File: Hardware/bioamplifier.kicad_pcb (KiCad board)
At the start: 4 copper layers, 71.8 x 45.1 mm, 97 parts, among them J1 Conn_01x07_Socket, J2 Conn_01x26_Pin, J3 Conn_01x07_Socket, J4 Jumper, J5 Jumper, U1 ADS1299IPAG, U10 TPD4E1B06DCKR, U11 LM2665M6, U2 TPD4E1B06DCKR, U3 TPD4E1B06DCKR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

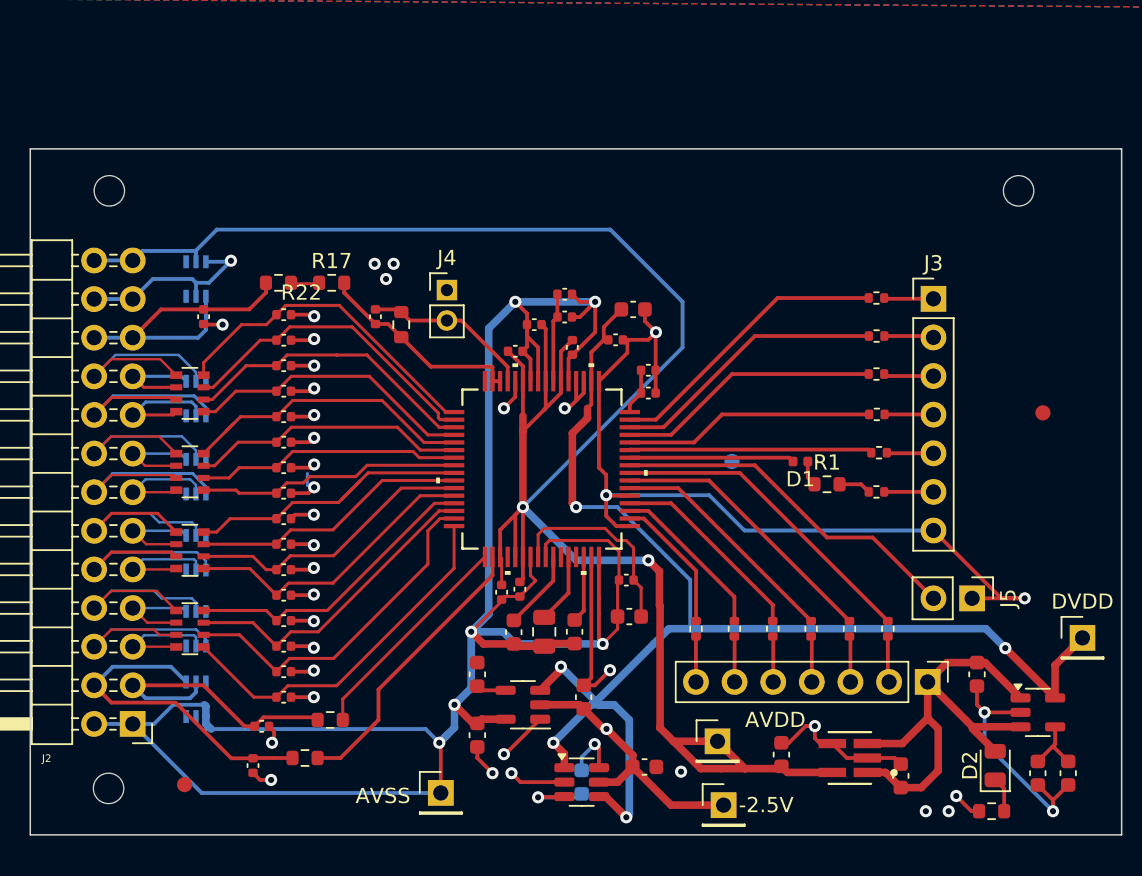
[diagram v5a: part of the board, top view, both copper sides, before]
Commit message: feat:begin rev3 with rp2350
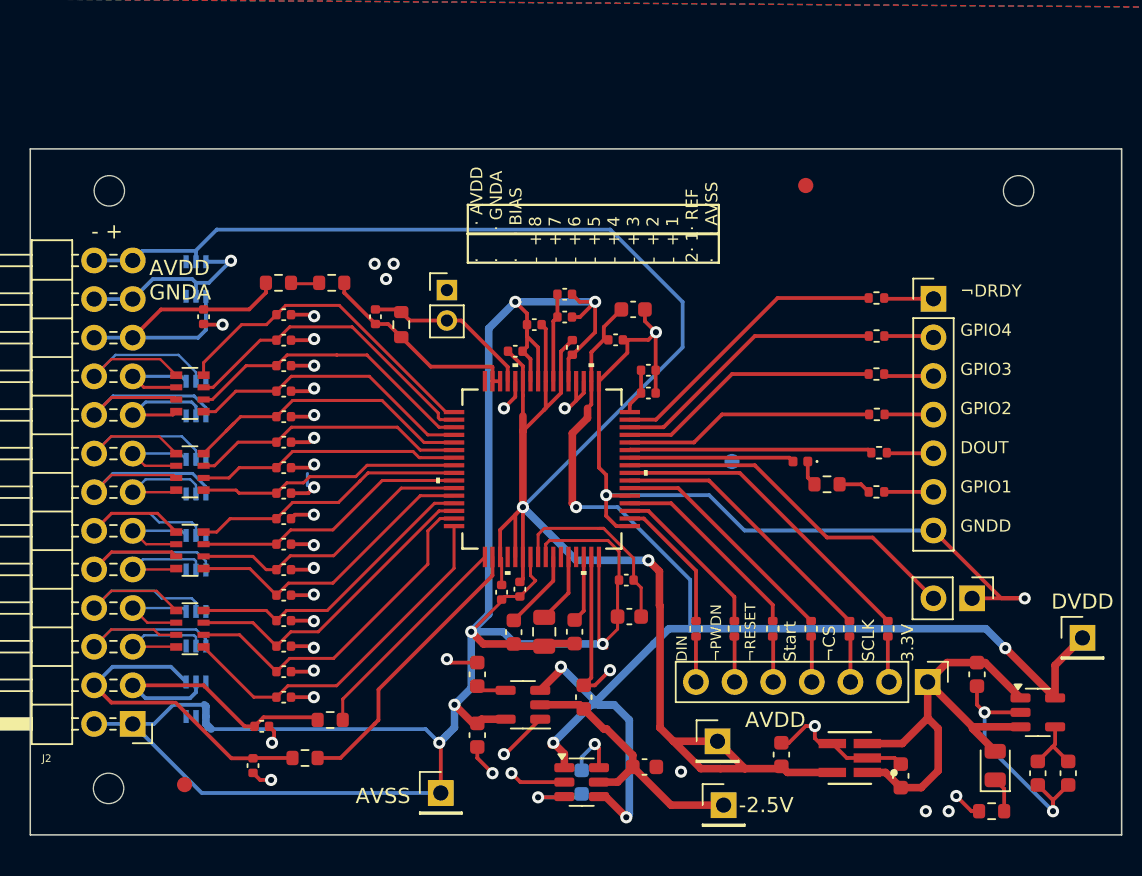
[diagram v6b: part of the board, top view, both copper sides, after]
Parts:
- moved FID3 21.6 mm to (101.6, 69.8)
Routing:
- net GNDA: track 76.5 -> 78.6 mm, vias 33 -> 34
- net IN4N: track 19.8 -> 18.1 mm
- net -2.5V_UNREG: vias 1 -> 0
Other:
- board text added: "- +"
- board text added: "AVDD GNDA"
- board text added: "DIN ¬PWDN ¬RESET"
- board text added: "Start ¬CS SCLK 3.3V"
- board text added: "¬DRDY GPIO4 GPIO3 GPIO2 DOUT GPIO1 GNDD"
- board text added: "· · AVDD · · GNDA · · BIAS - + 8 - + 7 - + 6 - + 5 - + 4 - + 3 - + 2 - + 1 2· 1· REF · · AVSS"
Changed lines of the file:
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@@
 			(drillshape 0)
 			(scaleselection 1)
-			(outputdirectory "Gerber/")
+			(outputdirectory "Gerber/drills/")
 		)
 	)
@@
 			(at 1.5 0.649034 0)
 			(layer "F.SilkS")
+			(hide yes)
 			(effects
 				(font
@@
 			(at 0 -1.17 0)
 			(layer "F.SilkS")
+			(hide yes)
 			(effects
 				(font
@@
 		)
 		(property "Value" "4.99 KΩ"
-			(at 0 1.43 0)
+			(at -0.67 3.5 0)
 			(layer "F.Fab")
 			(effects
@@
 			(at 0 -2.38 90)
 			(layer "F.SilkS")
+			(hide yes)
 			(effects
 				(font
@@
 		(tags "Through hole pin header THT 1x02 2.00mm single row")
 		(property "Reference" "J4"
-			(at 0 -2.11 0)
+			(at -0.53 -2.11 0)
 			(layer "F.SilkS")
+			(hide yes)
 			(effects
 				(font
@@
 			(at 0 -2.33 0)
 			(layer "F.SilkS")
+			(hide yes)
 			(effects
 				(font
@@
 			(at 0 -1.43 0)
 			(layer "F.SilkS")
+			(hide yes)
 			(effects
 				(font
@@
 	(footprint "Fiducial:Fiducial_1mm_Mask3mm"
 		(layer "F.Cu")
-		(at 117.2 84.8)
+		(at 101.6 69.85)
 		(descr "Circular Fiducial, 1mm bare copper, 3mm soldermask opening (recommended)")
 		(tags "fiducial")
@@
 			(at 0 -1.65 90)
 			(layer "F.SilkS")
+			(hide yes)
 			(effects
 				(font
@@
 			(at 0 -1.43 0)
 			(layer "F.SilkS")
+			(hide yes)
 			(effects
 				(font
@@
 	)
 	(gr_rect
+		(start 79.375 71.12)
+		(end 95.885 73.0504)
+		(stroke
+			(width 0.15)
+			(type default)
+		)
+		(fill no)
+		(layer "F.SilkS")
+	)
+	(gr_rect
+		(start 79.375 72.9996)
+		(end 95.885 74.93)
+		(stroke
+			(width 0.15)
+			(type default)
+		)
+		(fill no)
+		(layer "F.SilkS")
+	)
+	(gr_rect
 		(start 50.601596 67.442903)
 		(end 122.375 112.556276)
@@
 		(layer "Edge.Cuts")
 	)
+	(gr_text "DIN\n\n¬PWDN\n\n¬RESET\n\n"
+		(at 99.5 101.17 90)
+		(layer "F.SilkS")
+		(effects
+			(font
+				(size 0.7 0.7)
+				(thickness 0.15)
+			)
+			(justify left bottom)
+		)
+	)
+	(gr_text "¬DRDY\n\nGPIO4\n\nGPIO3\n\nGPIO2\n\nDOUT\n\nGPIO1\n\nGNDD"
+		(at 111.76 92.71 0)
+		(layer "F.SilkS")
+		(effects
+			(font
+				(size 0.8 0.8)
+				(thickness 0.15)
+			)
+			(justify left bottom)
+		)
+	)
+	(gr_text "·  	· AVDD\n· 	· GNDA\n·	· BIAS\n-  + 8\n-  + 7\n-  + 6\n-  + 5\n-  + 4\n-  + 3\n-  + 2\n-  + 1\n2· 1· REF\n·	· AVSS"
+		(at 95.885 74.93 90)
+		(layer "F.SilkS")
+		(effects
+			(font
+				(size 0.8 0.8)
+				(thickness 0.15)
+			)
+			(justify left bottom)
+		)
+	)
+	(gr_text "Start\n\n¬CS\n\nSCLK\n\n3.3V\n"
+		(at 108.766806 101.17 90)
+		(layer "F.SilkS")
+		(effects
+			(font
+				(size 0.8 0.8)
+				(thickness 0.15)
+			)
+			(justify left bottom)
+		)
+	)
+	(gr_text "- +\n"
+		(at 54.61 73.45 0)
+		(layer "F.SilkS")
+		(effects
+			(font
+				(size 1 1)
+				(thickness 0.15)
+			)
+			(justify left bottom)
+		)
+	)
+	(gr_text "AVDD \nGNDA\n"
+		(at 58.42 77.47 0)
+		(layer "F.SilkS")
+		(effects
+			(font
+				(size 1 1)
+				(thickness 0.15)
+			)
+			(justify left bottom)
+		)
+	)
 	(segment
 		(start 92.02 97.5)
@@
 	)
 	(segment
-		(start 90.28 93.68)
-		(end 90.28 95.8)
-		(width 0.2)
-		(layer "F.Cu")
-		(net 3)
-	)
-	(segment
 		(start 90.775 98.2)
 		(end 90.775 96.295)
@@
 	)
 	(segment
-		(start 89.8 93.2)
-		(end 90.28 93.68)
+		(start 84.4 92.4)
+		(end 88.309116 92.4)
 		(width 0.2)
 		(layer "F.Cu")
@@
 	)
 	(segment
-		(start 88.4 92.4)
-		(end 89.2 93.2)
+		(start 88.309116 92.4)
+		(end 88 92.4)
 		(width 0.2)
 		(layer "F.Cu")
@@
 	)
 	(segment
-		(start 84.4 92.4)
-		(end 88.4 92.4)
+		(start 84 94.2785)
+		(end 84 92.8)
 		(width 0.2)
 		(layer "F.Cu")
@@
 	)
 	(segment
-		(start 84 94.2785)
-		(end 84 92.8)
+		(start 90.28 94.370884)
+		(end 88.309116 92.4)
 		(width 0.2)
 		(layer "F.Cu")
@@
 	)
 	(segment
-		(start 89.2 93.2)
-		(end 89.8 93.2)
+		(start 90.28 95.8)
+		(end 90.28 94.370884)
 		(width 0.2)
 		(layer "F.Cu")
@@
 	)
 	(segment
+		(start 78.225 101.225)
+		(end 78 101)
+		(width 0.25)
+		(layer "F.Cu")
+		(net 4)
+	)
+	(segment
+		(start 80 101.225)
+		(end 78.225 101.225)
+		(width 0.25)
+		(layer "F.Cu")
+		(net 4)
+	)
+	(segment
 		(start 82.8375 109.0875)
 		(end 82.25 108.5)
@@
 		(net 4)
 	)
+	(via
+		(at 78 101)
+		(size 0.8)
+		(drill 0.4)
+		(layers "F.Cu" "B.Cu")
+		(free yes)
+		(net 4)
+	)
 	(segment
 		(start 58.66 76)
@@
 		(net 27)
 	)
-	(via
-		(at 88.5 105.5875)
-		(size 0.8)
-		(drill 0.4)
-		(layers "F.Cu" "B.Cu")
-		(net 27)
-	)
 	(segment
 		(start 89.225 98.2)
@@
 	)
 	(segment
-		(start 88 98)
-		(end 88 97)
-		(width 0.25)
-		(layer "F.Cu")
-		(net 28)
-	)
-	(segment
 		(start 80.275 104.95)
 		(end 80 105.225)
@@
 	)
 	(segment
-		(start 88 99.75)
-		(end 88 98)
-		(width 0.25)
-		(layer "F.Cu")
-		(net 28)
-	)
-	(segment
 		(start 84 80.5)
 		(end 84 82.7215)
@@
 	)
 	(segment
-		(start 88 97)
+		(start 88 99.75)
 		(end 88 94.2785)
-		(width 0.25)
+		(width 0.2)
 		(layer "F.Cu")
 		(net 28)
@@
 	)
 	(segment
-		(start 88.25 100)
-		(end 88 99.75)
-		(width 0.25)
-		(layer "F.Cu")
-		(net 28)
-	)
-	(segment
 		(start 86.75 78.5)
 		(end 87.75 77.5)
@@
 		(net 28)
 	)
+	(segment
+		(start 88.25 100)
+		(end 88 99.75)
+		(width 0.2)
+		(layer "F.Cu")
+		(net 28)
+	)
 	(via
 		(at 78.5 104)
@@
 		(width 0.2)
 		(layer "F.Cu")
-		(net 44)
-	)
-	(segment
-		(start 72.28355 89.28355)
-		(end 71.0671 90.5)
-		(width 0.2)
-		(layer "F.Cu")

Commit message: feat: fix Power pins
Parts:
- moved C21 1.17 mm to (80.5, 97.0)
- moved C3 1.03 mm to (90.5, 79.0), turned to 90 degrees
- moved C2 1.00 mm to (89.0, 81.0), turned to 90 degrees
- moved C23 0.75 mm to (87.0, 80.5)
- moved C6 0.50 mm to (85.8, 79.0), turned to 180 degrees
- moved C7 0.50 mm to (85.8, 77.5), turned to 180 degrees
- moved C1 0.45 mm to (83.0, 96.0), turned to 0 degrees
- moved C10 0.28 mm to (82.4, 99.5)
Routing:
- net DVDD: track 90.6 -> 120.0 mm
- net AVSS: track 152.8 -> 166.3 mm, vias 6 -> 7
- net AVDD: track 137.8 -> 149.7 mm, vias 2 -> 5
- net GNDD: track 77.6 -> 84.2 mm, vias 6 -> 7
- net Net-(U1-VCAP4): track 5.25 -> 6.63 mm
- net SRB1: track 14.6 -> 15.3 mm

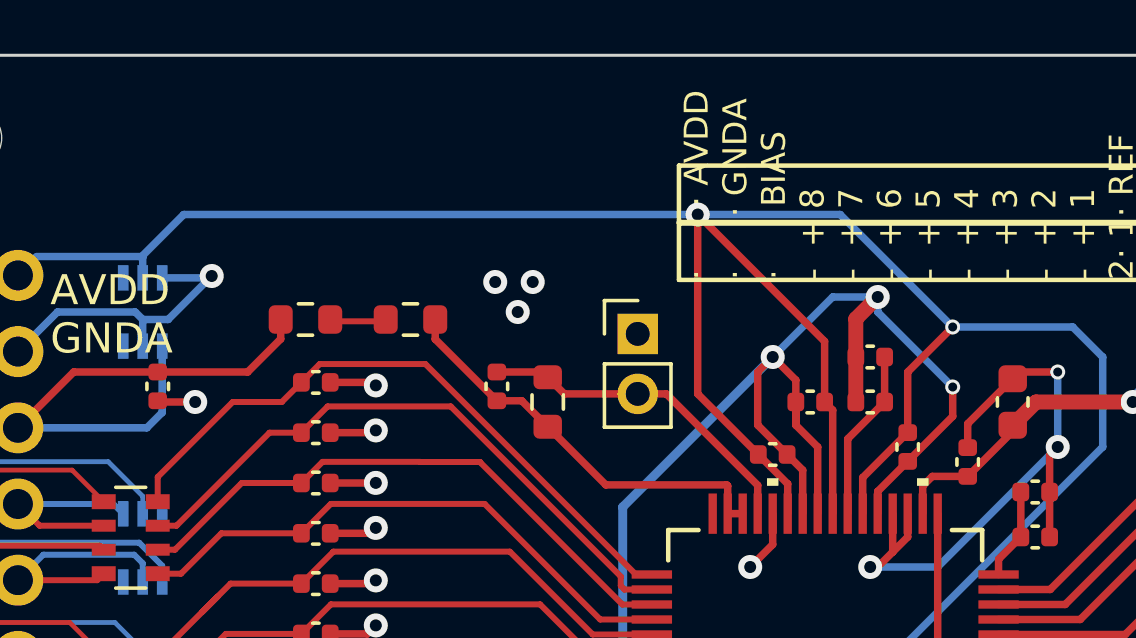
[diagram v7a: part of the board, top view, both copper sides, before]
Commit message: chore: small LDO Reg placement
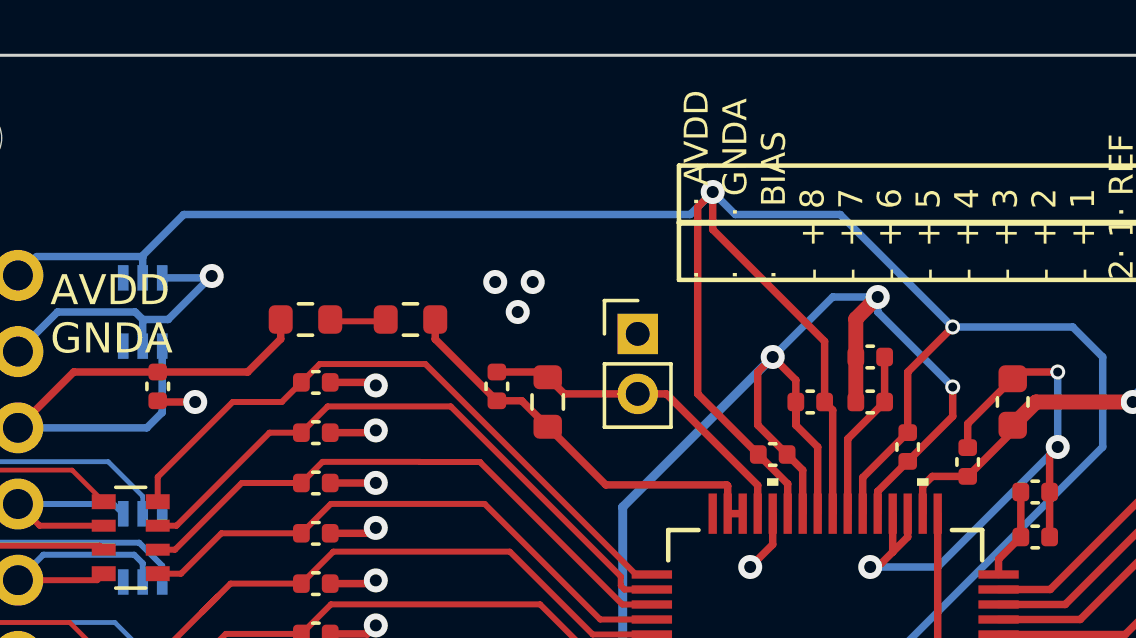
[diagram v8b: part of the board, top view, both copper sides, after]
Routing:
- net AVDD: track 149.7 -> 151.9 mm
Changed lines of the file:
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@@
-	)
-	(segment
-		(start 84.23 79)
-		(end 84.23 76.98)
-		(width 0.25)
-		(layer "F.Cu")
-		(net 1)
 	)
 	(segment
@@
 	)
 	(segment
+		(start 80.5 72)
+		(end 80 72.5)
+		(width 0.25)
+		(layer "F.Cu")
+		(net 1)
+	)
+	(segment
+		(start 80 78.73)
+		(end 82.02 80.75)
+		(width 0.25)
+		(layer "F.Cu")
+		(net 1)
+	)
+	(segment
 		(start 92.02 105.48)
 		(end 92.02 97.5)
@@
 	)
 	(segment
-		(start 80 78.73)
-		(end 80 72.75)
-		(width 0.25)
-		(layer "F.Cu")
-		(net 1)
-	)
-	(segment
 		(start 88.5 76.5)
 		(end 87 78)
@@
 	)
 	(segment
+		(start 80.5 72)
+		(end 80.5 73.25)
+		(width 0.25)
+		(layer "F.Cu")
+		(net 1)
+	)
+	(segment
 		(start 79.52 97.5)
 		(end 80.5 96.52)
@@
 	)
 	(segment
+		(start 84.23 76.98)
+		(end 84.23 79)
+		(width 0.25)
+		(layer "F.Cu")
+		(net 1)
+	)
+	(segment
 		(start 82.500001 94.2785)
 		(end 82.500001 95.980001)
@@
 	)
 	(segment
-		(start 82.02 80.75)
-		(end 80 78.73)
+		(start 80.5 73.25)
+		(end 84.23 76.98)
 		(width 0.25)
 		(layer "F.Cu")
@@
 	)
 	(segment
-		(start 84.23 76.98)
-		(end 80 72.75)
-		(width 0.25)
-		(layer "F.Cu")
-		(net 1)
-	)
-	(segment
 		(start 103.349517 108.450001)
 		(end 100.400001 108.450001)
@@
 		(start 82.52 96.163821)
 		(end 81.881214 96.802607)
+		(width 0.25)
+		(layer "F.Cu")
+		(net 1)
+	)
+	(segment
+		(start 80 72.5)
+		(end 80 78.73)
 		(width 0.25)
 		(layer "F.Cu")
@@
 	)
 	(via
-		(at 80 72.75)
+		(at 80.5 72)
 		(size 0.8)
 		(drill 0.4)
@@
 	)
 	(segment
+		(start 62.8679 72.75)
+		(end 61.465 74.1529)
+		(width 0.25)
+		(layer "B.Cu")
+		(net 1)
+	)
+	(segment
 		(start 61.465 74.1529)
 		(end 61.5 74.1879)
@@
 	)
 	(segment
+		(start 80.5 72)
+		(end 79.75 72.75)
+		(width 0.25)
+		(layer "B.Cu")
+		(net 1)
+	)
+	(segment
 		(start 79.5 97.5)
 		(end 79.5 94.5)
@@
 	)
 	(segment
-		(start 62.8679 72.75)
-		(end 61.465 74.1529)
-		(width 0.25)
-		(layer "B.Cu")
-		(net 1)
-	)
-	(segment
 		(start 61.5 74.1879)
 		(end 61.5 74.86335)
@@
 	)
 	(segment
+		(start 81.25 72.75)
+		(end 84.75 72.75)
+		(width 0.25)
+		(layer "B.Cu")
+		(net 1)
+	)
+	(segment
 		(start 86.5 94.5)
 		(end 83 91)
@@
 	)
 	(segment
+		(start 79.75 72.75)
+		(end 62.8679 72.75)
+		(width 0.25)
+		(layer "B.Cu")
+		(net 1)
+	)
+	(segment
 		(start 79.5 94.5)
 		(end 80.5 93.5)
@@
 	)
 	(segment
-		(start 80 72.75)
-		(end 62.8679 72.75)
-		(width 0.25)
-		(layer "B.Cu")
-		(net 1)
-	)
-	(segment
 		(start 80.5 95.5)
 		(end 82 97)
@@
 	)
 	(segment
-		(start 84.75 72.75)
-		(end 80 72.75)
+		(start 80.5 72)
+		(end 81.25 72.75)
 		(width 0.25)
 		(layer "B.Cu")
@@
 	)
 	(segment
+		(start 84.75 72.75)
+		(end 88.5 76.5)
+		(width 0.25)
+		(layer "B.Cu")
+		(net 1)
+	)
+	(segment
 		(start 88.5 76.5)
 		(end 92.5 76.5)
@@
 		(layer "B.Cu")
 		(net 1)
-	)
-	(segment
-		(start 88.5 76.5)
-		(end 84.75 72.75)
-		(width 0.25)
-		(layer "B.Cu")
-		(net 1)
